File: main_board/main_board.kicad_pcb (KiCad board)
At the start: 2 copper layers, 86 x 78.2 mm, 83 parts, among them J1 power, J2 debug, J3 led_matrix, J4 RJ45_LED_Shielded, J5 RJ45_LED_Shielded, J6 cathodes, J7 anodes, J8 power, Q1 SBC847AWT1G, Q10 2N7002P, Q11 2N7002P, Q12 SBC847AWT1G, Q13 SI2365EDS-T1-GE3, Q14 2N7002P, Q15 SBC847AWT1G, Q16 2N7002P, Q17 SI2365EDS-T1-GE3, Q18 SBC847AWT1G, Q19 2N7002P, Q2 SI2365EDS-T1-GE3, Q20 2N7002P, Q21 2N7002P, Q22 SI2365EDS-T1-GE3, Q23 2N7002P, Q24 SBC847AWT1G, Q25 SI2365EDS-T1-GE3, Q26 CPH3350-TL-W, Q3 SBC847AWT1G, Q4 2N7002P, Q5 SI2365EDS-T1-GE3, Q6 2N7002P, Q7 SBC847AWT1G, Q8 SI2365EDS-T1-GE3, Q9 2N7002P, U1 AP62250, U2 Pico, U3 AP62250

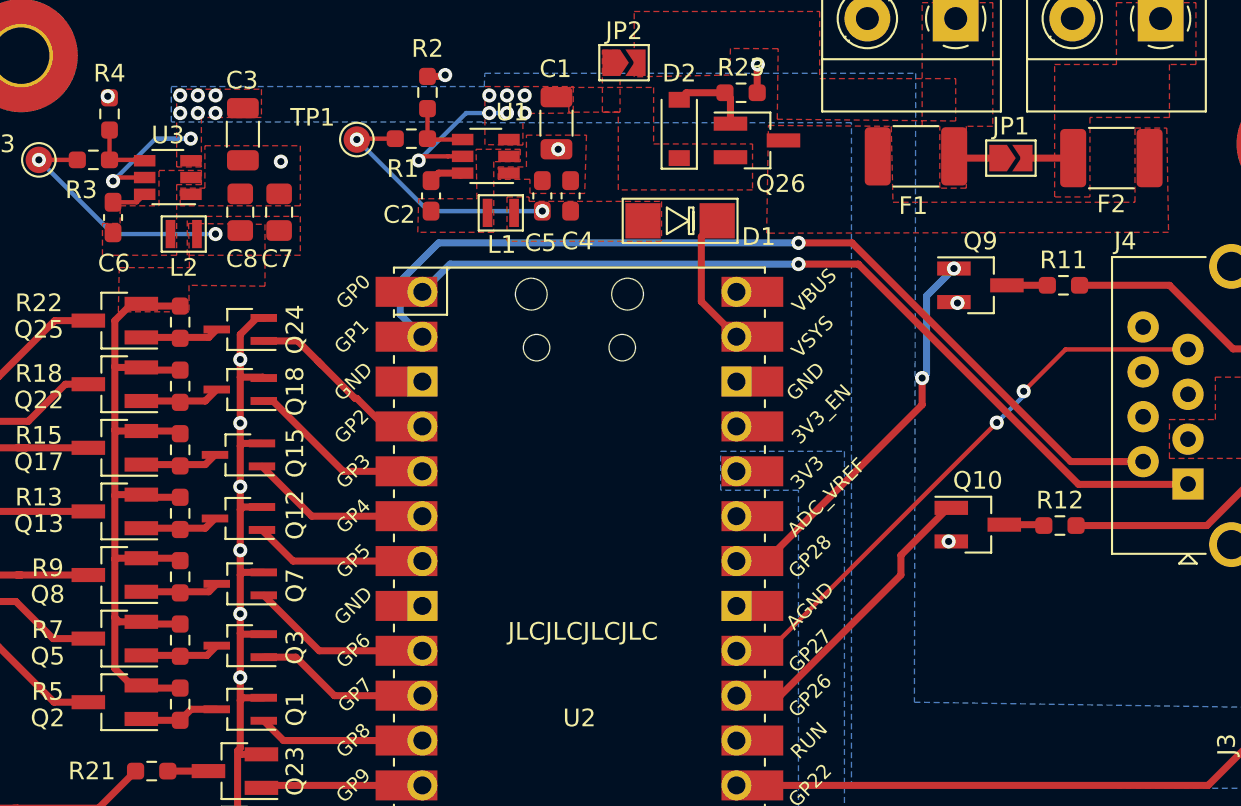
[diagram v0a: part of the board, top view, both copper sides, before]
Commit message: Rev2 of pcb that does not burn regulators
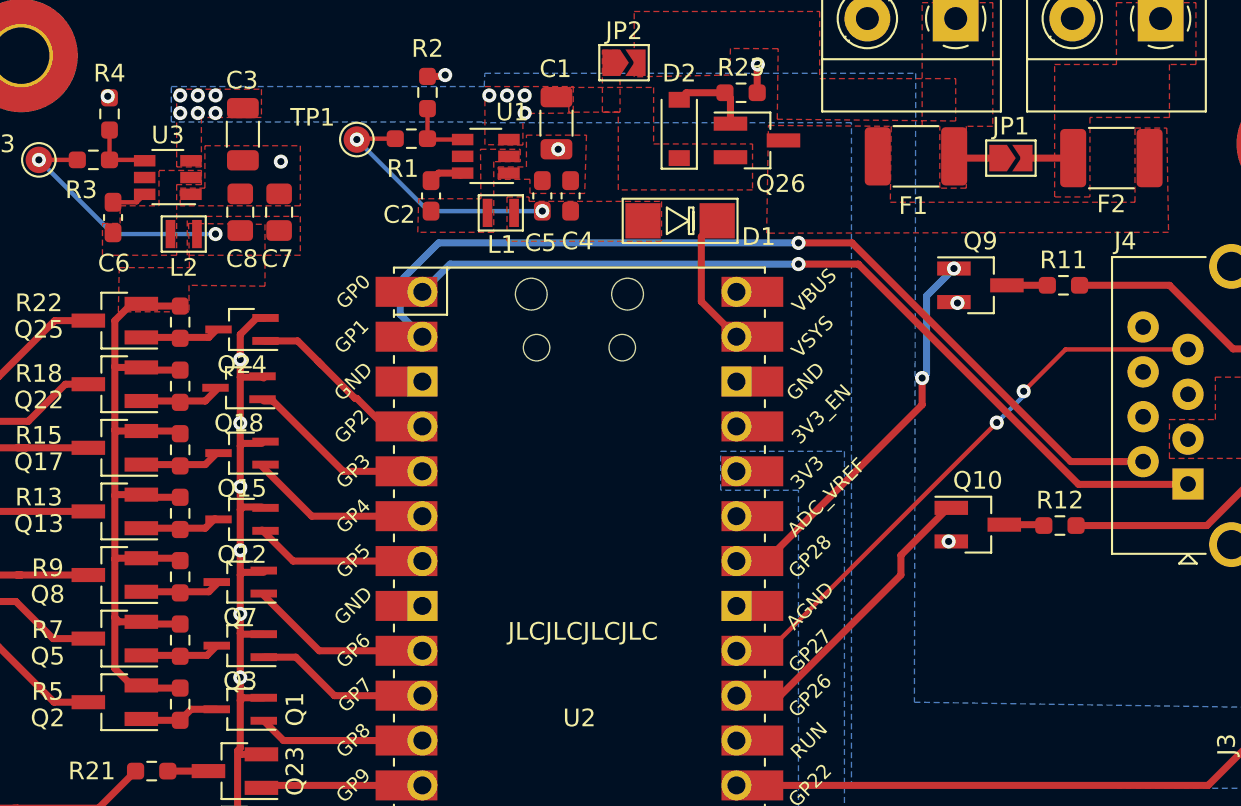
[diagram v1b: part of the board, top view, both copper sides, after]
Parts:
- Q1, Q12, Q15, Q18, Q24, Q3, Q7: value SBC847AWT1G -> BC848CWT1G
- moved Q15 0.22 mm to (91.5, 85.0)
- moved Q12 0.21 mm to (91.5, 88.8)
- moved Q18 0.12 mm to (91.3, 81.3)
- moved Q7 0.10 mm to (91.4, 92.3)
- moved Q24 0.10 mm to (91.5, 78.0)
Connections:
- J4 pad 4: Net-(J4-Pad4) -> (no net)
- J4 pad 5: Net-(J4-Pad5) -> (no net)
- J4 pad 6: Net-(J4-Pad6) -> (no net)
- J5 pad 4: Net-(J5-Pad4) -> (no net)
- J5 pad 5: Net-(J5-Pad5) -> (no net)
- J5 pad 6: Net-(J5-Pad6) -> (no net)
- U1 pad 5: vin -> (no net)
- U3 pad 5: vin -> (no net)
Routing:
- net vin: track 16.0 -> 0.00 mm, vias 15 -> 10
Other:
- board text added: "ETA Game System Main Board Rev2 Anton Lööf 2021"
- board text removed: "ETA Game System Main Board Anton Lööf 2021"

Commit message: refactoring and segment
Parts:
- Q1, Q12, Q15, Q18, Q24, Q3, Q7: value BC848CWT1G -> MCH3481-TL-W
- Q13, Q17, Q2, Q22, Q25, Q5, Q8: value SI2365EDS-T1-GE3 -> CPH3350-TL-W
- moved Q18 0.21 mm to (91.4, 81.5)
- moved Q24 0.14 mm to (91.4, 77.9)
- moved Q7 0.13 mm to (91.5, 92.3)
- moved Q12 0.11 mm to (91.6, 88.7)
- moved Q15 0.10 mm to (91.5, 85.1)
- moved Q3 0.09 mm to (91.5, 96.0)
